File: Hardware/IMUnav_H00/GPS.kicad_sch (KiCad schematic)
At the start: 0 parts

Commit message: Added GPS. Changes in power management.
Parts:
- added C1 (x2): 100n, Capacitor_SMD:C_0603_1608Metric, symbol Device:C
- added C2 (x2): 10u, Capacitor_SMD:C_0805_2012Metric, symbol Device:C
- added C48, C49: 1u, Capacitor_SMD:C_0603_1608Metric, symbol Device:C
- added FB3: GZ2012D101TF, Resistor_SMD:R_0805_2012Metric, symbol Device:FerriteBead_Small
- added J2: Conn_Coaxial, symbol Connector:Conn_Coaxial
- added R10 (x2): 100K, Resistor_SMD:R_0603_1608Metric, symbol Device:R
- added R30 (x2): 33R, Resistor_SMD:R_0603_1608Metric, symbol Device:R
- added R38: 10R, Resistor_SMD:R_0603_1608Metric, symbol Device:R
- added U13: NEO-M8U, RF_GPS:ublox_NEO, symbol RF_GPS:NEO-M8N
- added U15: XC6206P332MR, Package_TO_SOT_SMD:SOT-23-3, symbol Regulator_Linear:XC6206PxxxMR
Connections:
- new net: R30.2, U13.5 (USB_DM)
- new net: C2.1, FB3.1, R38.2
- new net: FB3.2, J2.1 (In), U13.11 (RF_IN)
- new net: R38.1, U13.9 (VCC_RF)
- new net: R30.2, U13.6 (USB_DP)
- new net: C49.1, R10.1, U13.7 (VDD_USB), U15.2 (VO)
- new net +3V3: C1.1, C2.1, R10.1, U13.2 (D_SEL), U13.23 (VCC)
- new net +5V: C48.1, U15.3 (VI)
- new net GND: C1.2, C1.2, C2.2, C2.2, C48.2, C49.2, J2.2 (Ext), R10.2, U13.10 (GND), U13.12 (GND), U13.13 (GND), U13.24 (GND), U15.1 (GND)
- new net GPS_BCKP_POWER: C1.1, U13.22 (V_BCKP)
- new net GPS_D+: R30.1
- new net GPS_D-: R30.1
- new net GPS_EXTINT: U13.4 (EXTINT)
- new net GPS_RX: U13.21 (RXD/SPI_MOSI)
- new net GPS_TIMEPULSE: U13.3 (TIMEPULSE)
- new net GPS_TX: U13.20 (TXD/SPI_MISO)
- new net GPS_~{RESET}: R10.2, U13.8 (~{RESET})
- no-connect marks 0 -> 4
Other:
- note added: "Designed for use with active GPS antenna"

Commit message: Finalized and cleaned Power Management, added GPS antenna footprint
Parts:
- J2: footprint (none) -> Connector_Coaxial:SMA_Amphenol_901-143_Horizontal
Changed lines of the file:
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@@
       (effects (font (size 1.27 1.27)) (justify left))
     )
-    (property "Footprint" "" (at 207.01 73.66 0)
+    (property "Footprint" "Connector_Coaxial:SMA_Amphenol_901-143_Horizontal" (at 207.01 73.66 0)
       (effects (font (size 1.27 1.27)) hide)
     )

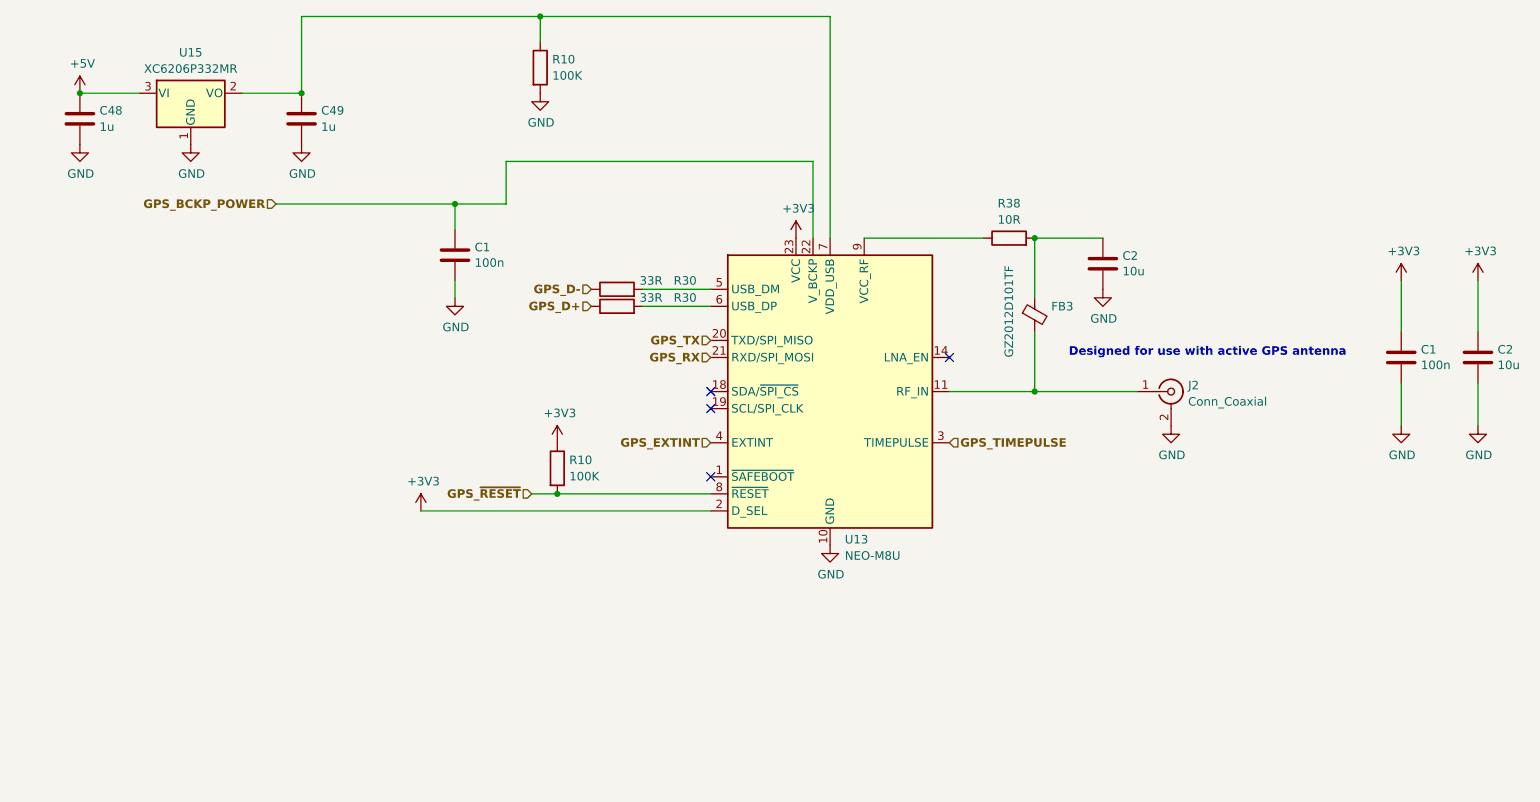
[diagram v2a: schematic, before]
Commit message: Added signal connections to MCU+misc
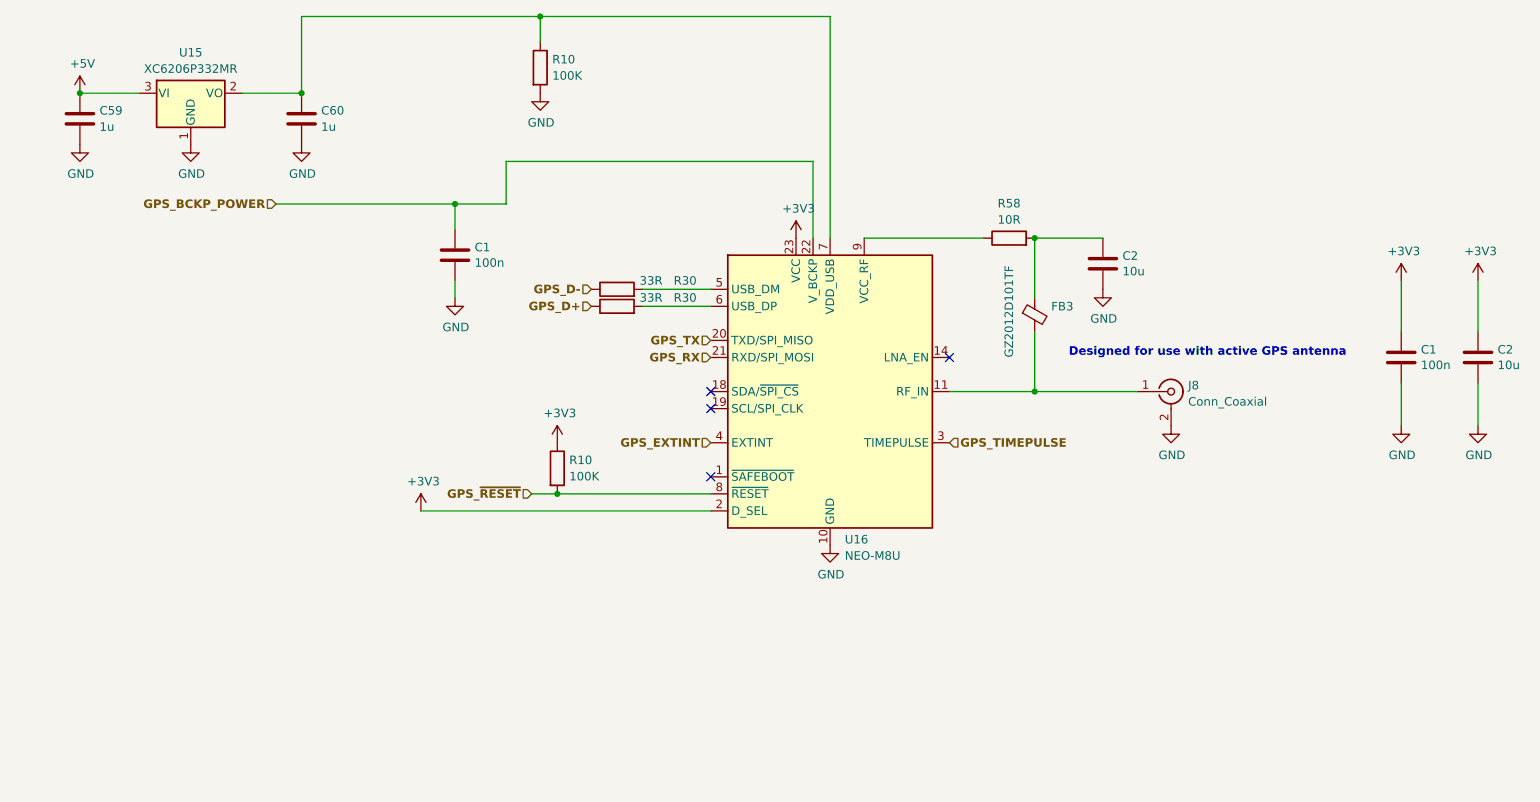
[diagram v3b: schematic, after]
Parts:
- renumbered C48 to C59, C49 to C60, J2 to J8, R38 to R58, U13 to U16
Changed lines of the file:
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@@
         )
         (path "/4c2dd95e-3649-4040-ab57-00df6d22e0b0/61a7e487-220c-46a1-aef5-176736fd02e1"
-          (reference "R32") (unit 1)
+          (reference "R56") (unit 1)
         )
       )
@@
         )
         (path "/4c2dd95e-3649-4040-ab57-00df6d22e0b0/61a7e487-220c-46a1-aef5-176736fd02e1"
-          (reference "#PWR0142") (unit 1)
+          (reference "#PWR0202") (unit 1)
         )
       )
@@
   (symbol (lib_id "Connector:Conn_Coaxial") (at 207.01 73.66 0) (unit 1)
     (in_bom yes) (on_board yes) (dnp no) (fields_autoplaced)
-    (property "Reference" "J2" (at 209.5501 72.7411 0)
+    (property "Reference" "J8" (at 209.5501 72.7411 0)
       (effects (font (size 1.27 1.27)) (justify left))
     )
@@
       (project "IMUnav_H00"
         (path "/4c2dd95e-3649-4040-ab57-00df6d22e0b0/61a7e487-220c-46a1-aef5-176736fd02e1"
-          (reference "J2") (unit 1)
+          (reference "J8") (unit 1)
         )
       )
@@
         )
         (path "/4c2dd95e-3649-4040-ab57-00df6d22e0b0/61a7e487-220c-46a1-aef5-176736fd02e1"
-          (reference "#PWR0149") (unit 1)
+          (reference "#PWR0193") (unit 1)
         )
       )
@@
         )
         (path "/4c2dd95e-3649-4040-ab57-00df6d22e0b0/61a7e487-220c-46a1-aef5-176736fd02e1"
-          (reference "#PWR0143") (unit 1)
+          (reference "#PWR0196") (unit 1)
         )
       )
@@
         )
         (path "/4c2dd95e-3649-4040-ab57-00df6d22e0b0/61a7e487-220c-46a1-aef5-176736fd02e1"
-          (reference "C53") (unit 1)
+          (reference "C61") (unit 1)
         )
       )
@@
         )
         (path "/4c2dd95e-3649-4040-ab57-00df6d22e0b0/61a7e487-220c-46a1-aef5-176736fd02e1"
-          (reference "#PWR0150") (unit 1)
+          (reference "#PWR0191") (unit 1)
         )
       )
@@
         )
         (path "/4c2dd95e-3649-4040-ab57-00df6d22e0b0/61a7e487-220c-46a1-aef5-176736fd02e1"
-          (reference "#PWR0148") (unit 1)
+          (reference "#PWR0195") (unit 1)
         )
       )
@@
         )
         (path "/4c2dd95e-3649-4040-ab57-00df6d22e0b0/61a7e487-220c-46a1-aef5-176736fd02e1"
-          (reference "C52") (unit 1)
+          (reference "C62") (unit 1)
         )
       )
@@
         )
         (path "/4c2dd95e-3649-4040-ab57-00df6d22e0b0/61a7e487-220c-46a1-aef5-176736fd02e1"
-          (reference "R37") (unit 1)
+          (reference "R55") (unit 1)
         )
       )
@@
         )
         (path "/4c2dd95e-3649-4040-ab57-00df6d22e0b0/61a7e487-220c-46a1-aef5-176736fd02e1"
-          (reference "#PWR0157") (unit 1)
+          (reference "#PWR0192") (unit 1)
         )
       )
@@
   (symbol (lib_id "Device:R") (at 182.88 50.8 90) (unit 1)
     (in_bom yes) (on_board yes) (dnp no) (fields_autoplaced)
-    (property "Reference" "R38" (at 182.88 45.6397 90)
+    (property "Reference" "R58" (at 182.88 45.6397 90)
       (effects (font (size 1.27 1.27)))
     )
@@
       (project "IMUnav_H00"
         (path "/4c2dd95e-3649-4040-ab57-00df6d22e0b0/61a7e487-220c-46a1-aef5-176736fd02e1"
-          (reference "R38") (unit 1)
+          (reference "R58") (unit 1)
         )
       )
@@
   (symbol (lib_id "RF_GPS:NEO-M8N") (at 156.21 73.66 0) (unit 1)
     (in_bom yes) (on_board yes) (dnp no) (fields_autoplaced)
-    (property "Reference" "U13" (at 158.4041 95.7001 0)
+    (property "Reference" "U16" (at 158.4041 95.7001 0)
       (effects (font (size 1.27 1.27)) (justify left))
     )
@@
       (project "IMUnav_H00"
         (path "/4c2dd95e-3649-4040-ab57-00df6d22e0b0/61a7e487-220c-46a1-aef5-176736fd02e1"
-          (reference "U13") (unit 1)
+          (reference "U16") (unit 1)
         )
       )
@@
         )
         (path "/4c2dd95e-3649-4040-ab57-00df6d22e0b0/61a7e487-220c-46a1-aef5-176736fd02e1"
-          (reference "R36") (unit 1)
+          (reference "R54") (unit 1)
         )
       )
@@
         )
         (path "/4c2dd95e-3649-4040-ab57-00df6d22e0b0/61a7e487-220c-46a1-aef5-176736fd02e1"
-          (reference "#PWR0144") (unit 1)
+          (reference "#PWR0190") (unit 1)
         )
       )
@@
         )
         (path "/4c2dd95e-3649-4040-ab57-00df6d22e0b0/61a7e487-220c-46a1-aef5-176736fd02e1"
-          (reference "#PWR0145") (unit 1)
+          (reference "#PWR0189") (unit 1)
         )
       )
@@
   (symbol (lib_id "Device:C") (at 44.45 33.02 0) (unit 1)
     (in_bom yes) (on_board yes) (dnp no) (fields_autoplaced)
-    (property "Reference" "C48" (at 47.371 31.8079 0)
+    (property "Reference" "C59" (at 47.371 31.8079 0)
       (effects (font (size 1.27 1.27)) (justify left))
     )
@@
       (project "IMUnav_H00"
         (path "/4c2dd95e-3649-4040-ab57-00df6d22e0b0/61a7e487-220c-46a1-aef5-176736fd02e1"
-          (reference "C48") (unit 1)
+          (reference "C59") (unit 1)
         )
       )
@@
         )
         (path "/4c2dd95e-3649-4040-ab57-00df6d22e0b0/61a7e487-220c-46a1-aef5-176736fd02e1"
-          (reference "C47") (unit 1)
+          (reference "C64") (unit 1)
         )
       )
@@
         )
         (path "/4c2dd95e-3649-4040-ab57-00df6d22e0b0/61a7e487-220c-46a1-aef5-176736fd02e1"
-          (reference "#PWR0146") (unit 1)
+          (reference "#PWR0188") (unit 1)
         )
       )
@@
         )
         (path "/4c2dd95e-3649-4040-ab57-00df6d22e0b0/61a7e487-220c-46a1-aef5-176736fd02e1"
-          (reference "C46") (unit 1)
+          (reference "C63") (unit 1)
         )
       )
@@
         )
         (path "/4c2dd95e-3649-4040-ab57-00df6d22e0b0/61a7e487-220c-46a1-aef5-176736fd02e1"
-          (reference "#PWR0152") (unit 1)
+          (reference "#PWR0198") (unit 1)
         )
       )
@@
   (symbol (lib_id "Device:C") (at 77.47 33.02 0) (unit 1)
     (in_bom yes) (on_board yes) (dnp no) (fields_autoplaced)
-    (property "Reference" "C49" (at 80.391 31.8079 0)
+    (property "Reference" "C60" (at 80.391 31.8079 0)
       (effects (font (size 1.27 1.27)) (justify left))
     )
@@
       (project "IMUnav_H00"
         (path "/4c2dd95e-3649-4040-ab57-00df6d22e0b0/61a7e487-220c-46a1-aef5-176736fd02e1"
-          (reference "C49") (unit 1)
+          (reference "C60") (unit 1)
         )
       )
@@
         )
         (path "/4c2dd95e-3649-4040-ab57-00df6d22e0b0/61a7e487-220c-46a1-aef5-176736fd02e1"
-          (reference "#PWR0139") (unit 1)
+          (reference "#PWR0199") (unit 1)
         )
       )
@@
         )
         (path "/4c2dd95e-3649-4040-ab57-00df6d22e0b0/61a7e487-220c-46a1-aef5-176736fd02e1"
-          (reference "#PWR0156") (unit 1)
+          (reference "#PWR0197") (unit 1)
         )
       )
@@
         )
         (path "/4c2dd95e-3649-4040-ab57-00df6d22e0b0/61a7e487-220c-46a1-aef5-176736fd02e1"
-          (reference "#PWR0147") (unit 1)
+          (reference "#PWR0187") (unit 1)
         )
       )
@@
         )
         (path "/4c2dd95e-3649-4040-ab57-00df6d22e0b0/61a7e487-220c-46a1-aef5-176736fd02e1"
-          (reference "#PWR0141") (unit 1)
+          (reference "#PWR0201") (unit 1)
         )
       )
@@
         )
         (path "/4c2dd95e-3649-4040-ab57-00df6d22e0b0/61a7e487-220c-46a1-aef5-176736fd02e1"
-          (reference "#PWR0140") (unit 1)
+          (reference "#PWR0200") (unit 1)
         )
       )
@@
         )
         (path "/4c2dd95e-3649-4040-ab57-00df6d22e0b0/61a7e487-220c-46a1-aef5-176736fd02e1"
-          (reference "R33") (unit 1)
+          (reference "R57") (unit 1)
         )
       )
@@
         )
         (path "/4c2dd95e-3649-4040-ab57-00df6d22e0b0/61a7e487-220c-46a1-aef5-176736fd02e1"
-          (reference "#PWR0151") (unit 1)
-        )
-      )
+          (reference "#PWR0194") (unit 1)
+        )
+      )

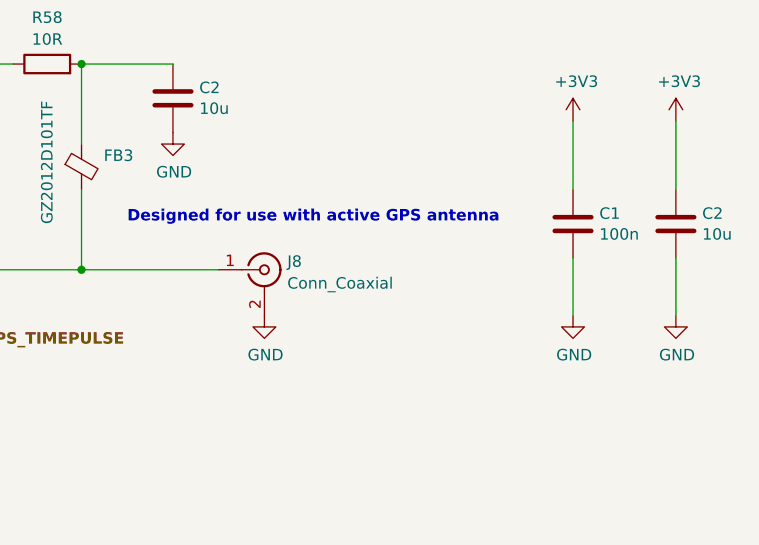
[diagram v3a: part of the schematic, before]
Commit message: PCB layout - BGA fanout, GPS and USB hub
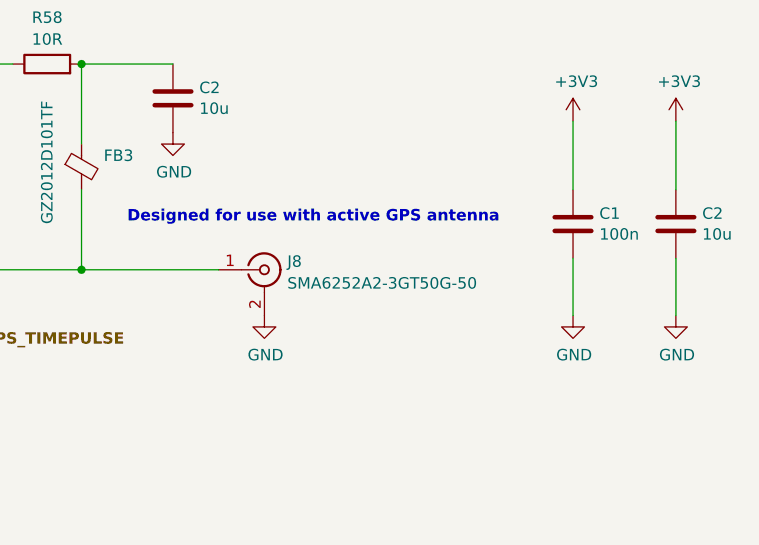
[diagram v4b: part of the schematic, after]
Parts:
- J8: value Conn_Coaxial -> SMA6252A2-3GT50G-50
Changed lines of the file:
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@@
       (effects (font (size 1.27 1.27)) (justify left))
     )
-    (property "Value" "Conn_Coaxial" (at 209.5501 75.1653 0)
+    (property "Value" "SMA6252A2-3GT50G-50\n" (at 209.5501 75.1653 0)
       (effects (font (size 1.27 1.27)) (justify left))
     )
